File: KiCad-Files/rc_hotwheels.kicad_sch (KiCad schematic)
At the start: 2 parts, among them U1 STM32F070F6P6

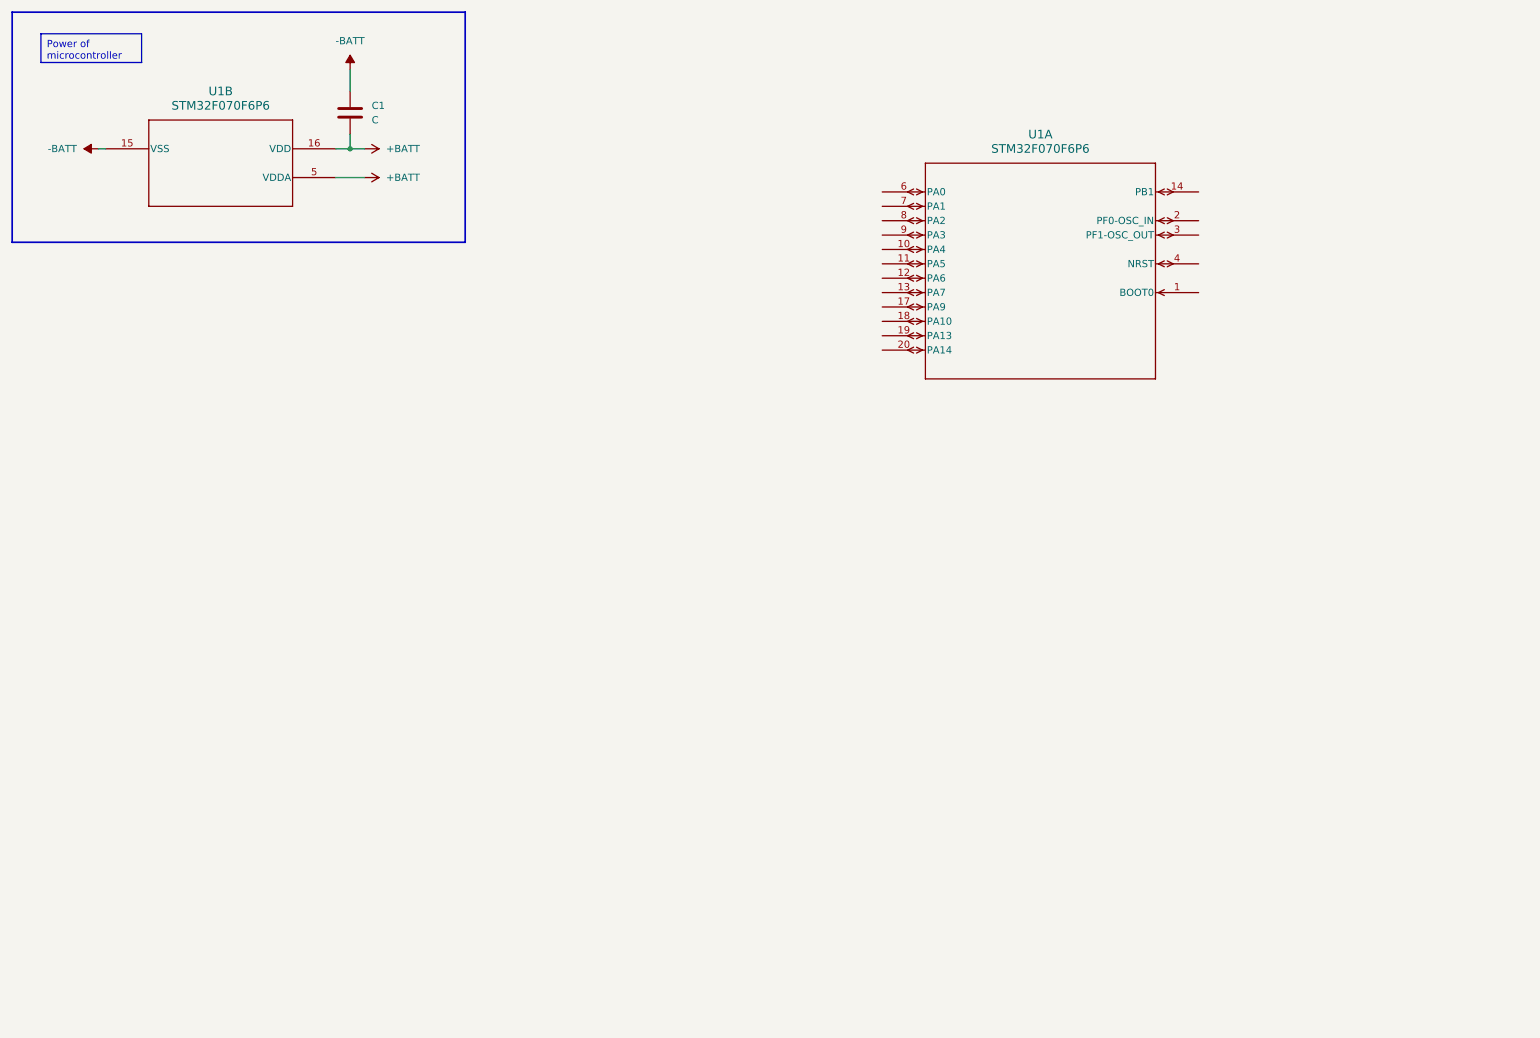
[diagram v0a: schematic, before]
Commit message: Added H-Bridge symbol and connection.
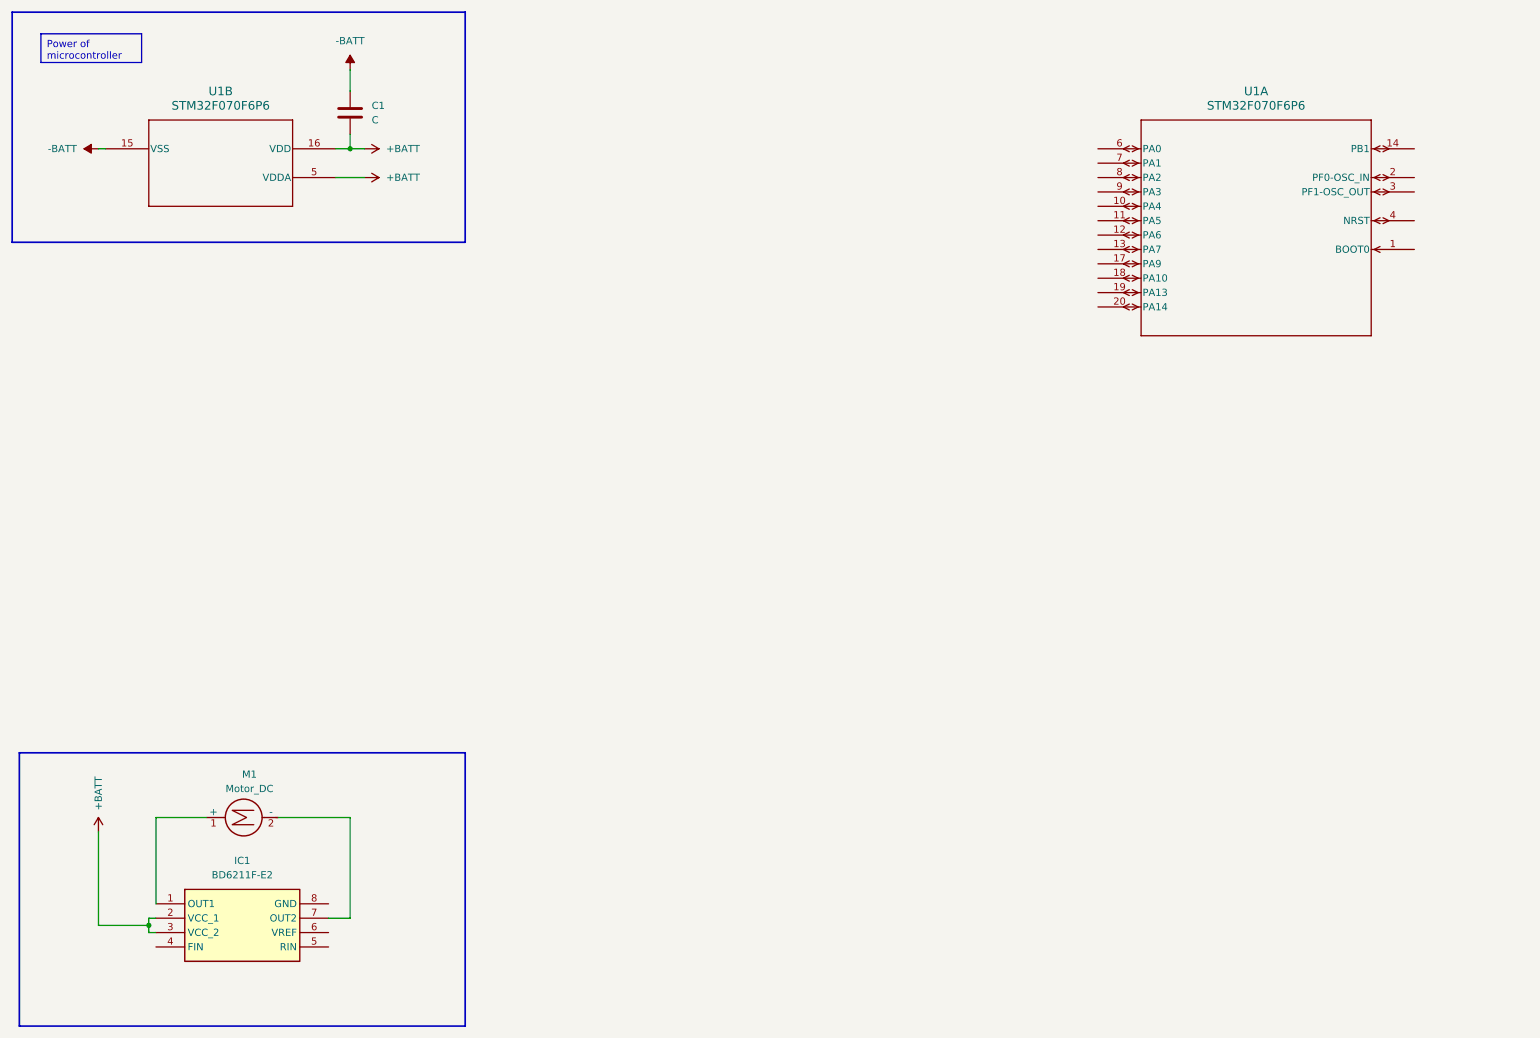
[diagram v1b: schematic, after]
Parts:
- added IC1: BD6211F-E2, SOIC127P620X171-8N, symbol SamacSys_Parts:BD6211F-E2
- added M1: Motor_DC, symbol Motor:Motor_DC
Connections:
- net +BATT: now also IC1.2 (VCC_1), IC1.3 (VCC_2)
- new net: IC1.1 (OUT1), M1.1 (+)
- new net: IC1.7 (OUT2), M1.2 (-)
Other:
- moved on the sheet: U1A
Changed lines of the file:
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@@
   (junction (at 74.93 39.37) (diameter 0) (color 0 0 0 0)
   )
+  (junction (at 39.37 176.53) (diameter 0) (color 0 0 0 0)
+  )
   (wire (pts (xy 74.93 39.37) (xy 77.47 39.37))
     (stroke (width 0) (type default))
   )
+  (wire (pts (xy 71.12 175.26) (xy 74.93 175.26))
+    (stroke (width 0) (type default))
+  )
+  (wire (pts (xy 40.64 172.72) (xy 40.64 157.48))
+    (stroke (width 0) (type default))
+  )
   (wire (pts (xy 74.93 36.83) (xy 74.93 39.37))
     (stroke (width 0) (type default))
@@
     (stroke (width 0) (type default))
   )
+  (wire (pts (xy 39.37 177.8) (xy 39.37 176.53))
+    (stroke (width 0) (type default))
+  )
+  (wire (pts (xy 39.37 175.26) (xy 40.64 175.26))
+    (stroke (width 0) (type default))
+  )
+  (wire (pts (xy 40.64 177.8) (xy 39.37 177.8))
+    (stroke (width 0) (type default))
+  )
+  (wire (pts (xy 39.37 176.53) (xy 39.37 175.26))
+    (stroke (width 0) (type default))
+  )
+  (wire (pts (xy 62.23 157.48) (xy 74.93 157.48))
+    (stroke (width 0) (type default))
+  )
   (wire (pts (xy 72.39 44.45) (xy 77.47 44.45))
     (stroke (width 0) (type default))
   )
+  (wire (pts (xy 40.64 157.48) (xy 49.53 157.48))
+    (stroke (width 0) (type default))
+  )
   (wire (pts (xy 30.48 39.37) (xy 31.75 39.37))
     (stroke (width 0) (type default))
   )
+  (wire (pts (xy 74.93 157.48) (xy 74.93 175.26))
+    (stroke (width 0) (type default))
+  )
+  (wire (pts (xy 30.48 176.53) (xy 39.37 176.53))
+    (stroke (width 0) (type default))
+  )
   (wire (pts (xy 72.39 39.37) (xy 74.93 39.37))
     (stroke (width 0) (type default))
   )
+  (wire (pts (xy 30.48 160.02) (xy 30.48 176.53))
+    (stroke (width 0) (type default))
+  )
   (rectangle (start 15.24 15.24) (end 95.25 55.88)
+    (stroke (width 0.3) (type solid) (color 0 0 0 1))
+    (fill (type none))
+  )
+  (rectangle (start 16.51 146.05) (end 95.25 194.31)
     (stroke (width 0.3) (type solid) (color 0 0 0 1))
     (fill (type none))
@@
     )
   )
-  (symbol (lib_id "2023-11-22_23-54-19:STM32F070F6P6") (at 168.91 46.99 0) (unit 1)
-    (in_bom yes) (on_board yes) (dnp no) (fields_autoplaced)
-    (property "Reference" "U1" (at 196.85 36.83 0)
+  (symbol (lib_id "2023-11-22_23-54-19:STM32F070F6P6") (at 207.01 39.37 0) (unit 1)
+    (in_bom yes) (on_board yes) (dnp no) (fields_autoplaced)
+    (property "Reference" "U1" (at 234.95 29.21 0)
       (effects (font (size 1.524 1.524)))
     )
-    (property "Value" "STM32F070F6P6" (at 196.85 39.37 0)
+    (property "Value" "STM32F070F6P6" (at 234.95 31.75 0)
       (effects (font (size 1.524 1.524)))
     )
-    (property "Footprint" "TSSOP20" (at 168.91 46.99 0)
+    (property "Footprint" "TSSOP20" (at 207.01 39.37 0)
       (effects (font (size 1.27 1.27) italic) hide)
     )
-    (property "Datasheet" "STM32F070F6P6" (at 168.91 46.99 0)
+    (property "Datasheet" "STM32F070F6P6" (at 207.01 39.37 0)
       (effects (font (size 1.27 1.27) italic) hide)
     )
@@
     )
   )
+  (symbol (lib_id "power:+BATT") (at 30.48 160.02 0) (unit 1)
+    (in_bom yes) (on_board yes) (dnp no)
+    (property "Reference" "#PWR05" (at 30.48 163.83 0)
+      (effects (font (size 1.27 1.27)) hide)
+    )
+    (property "Value" "+BATT" (at 30.48 156.21 90)
+      (effects (font (size 1.27 1.27)) (justify left))
+    )
+    (property "Footprint" "" (at 30.48 160.02 0)
+      (effects (font (size 1.27 1.27)) hide)
+    )
+    (property "Datasheet" "" (at 30.48 160.02 0)
+      (effects (font (size 1.27 1.27)) hide)
+    )
+    (pin "1")
+    (instances
+      (project "rc_hotwheels"
+        (path "/0b835094-f9c0-45ab-a312-d1f27d043c8e"
+          (reference "#PWR05") (unit 1)
+        )
+      )
+    )
+  )
+  (symbol (lib_id "Motor:Motor_DC") (at 54.61 157.48 90) (unit 1)
+    (in_bom yes) (on_board yes) (dnp no) (fields_autoplaced)
+    (property "Reference" "M1" (at 57.15 149.86 90)
+      (effects (font (size 1.27 1.27)))
+    )
+    (property "Value" "Motor_DC" (at 57.15 152.4 90)
+      (effects (font (size 1.27 1.27)))
+    )
+    (property "Footprint" "" (at 56.896 157.48 0)
+      (effects (font (size 1.27 1.27)) hide)
+    )
+    (property "Datasheet" "~" (at 56.896 157.48 0)
+      (effects (font (size 1.27 1.27)) hide)
+    )
+    (pin "1")
+    (pin "2")
+    (instances
+      (project "rc_hotwheels"
+        (path "/0b835094-f9c0-45ab-a312-d1f27d043c8e"
+          (reference "M1") (unit 1)
+        )
+      )
+    )
+  )
   (symbol (lib_id "power:-BATT") (at 30.48 39.37 90) (unit 1)
     (in_bom yes) (on_board yes) (dnp no) (fields_autoplaced)
@@
         )
       )
+    )
+  )
+  (symbol (lib_id "SamacSys_Parts:BD6211F-E2") (at 40.64 172.72 0) (unit 1)
+    (in_bom yes) (on_board yes) (dnp no) (fields_autoplaced)
+    (property "Reference" "IC1" (at 55.88 165.1 0)
+      (effects (font (size 1.27 1.27)))
+    )
+    (property "Value" "BD6211F-E2" (at 55.88 167.64 0)
+      (effects (font (size 1.27 1.27)))
+    )
+    (property "Footprint" "SOIC127P620X171-8N" (at 67.31 267.64 0)
+      (effects (font (size 1.27 1.27)) (justify left top) hide)
+    )
+    (property "Datasheet" "https://datasheet.datasheetarchive.com/originals/distributors/Datasheets_SAMA/9ec5cdfbd612023d7489950ca9dee0a8.pdf" (at 67.31 367.64 0)
+      (effects (font (size 1.27 1.27)) (justify left top) hide)
+    )
+    (property "Height" "1.71" (at 67.31 567.64 0)
+      (effects (font (size 1.27 1.27)) (justify left top) hide)
+    )
+    (property "Farnell Part Number" "" (at 67.31 667.64 0)
+      (effects (font (size 1.27 1.27)) (justify left top) hide)
+    )
+    (property "Farnell Price/Stock" "" (at 67.31 767.64 0)
+      (effects (font (size 1.27 1.27)) (justify left top) hide)
+    )
+    (property "Manufacturer_Name" "ROHM Semiconductor" (at 67.31 867.64 0)
+      (effects (font (size 1.27 1.27)) (justify left top) hide)
+    )
+    (property "Manufacturer_Part_Number" "BD6211F-E2" (at 67.31 967.64 0)
+      (effects (font (size 1.27 1.27)) (justify left top) hide)
+    )
+    (pin "1")
+    (pin "2")
+    (pin "3")
+    (pin "4")
+    (pin "5")
+    (pin "6")
+    (pin "7")
+    (pin "8")
+    (instances
+      (project "rc_hotwheels"
+        (path "/0b835094-f9c0-45ab-a312-d1f27d043c8e"
+          (reference "IC1") (unit 1)
+        )
+      )

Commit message: Added receiver symbol and connections
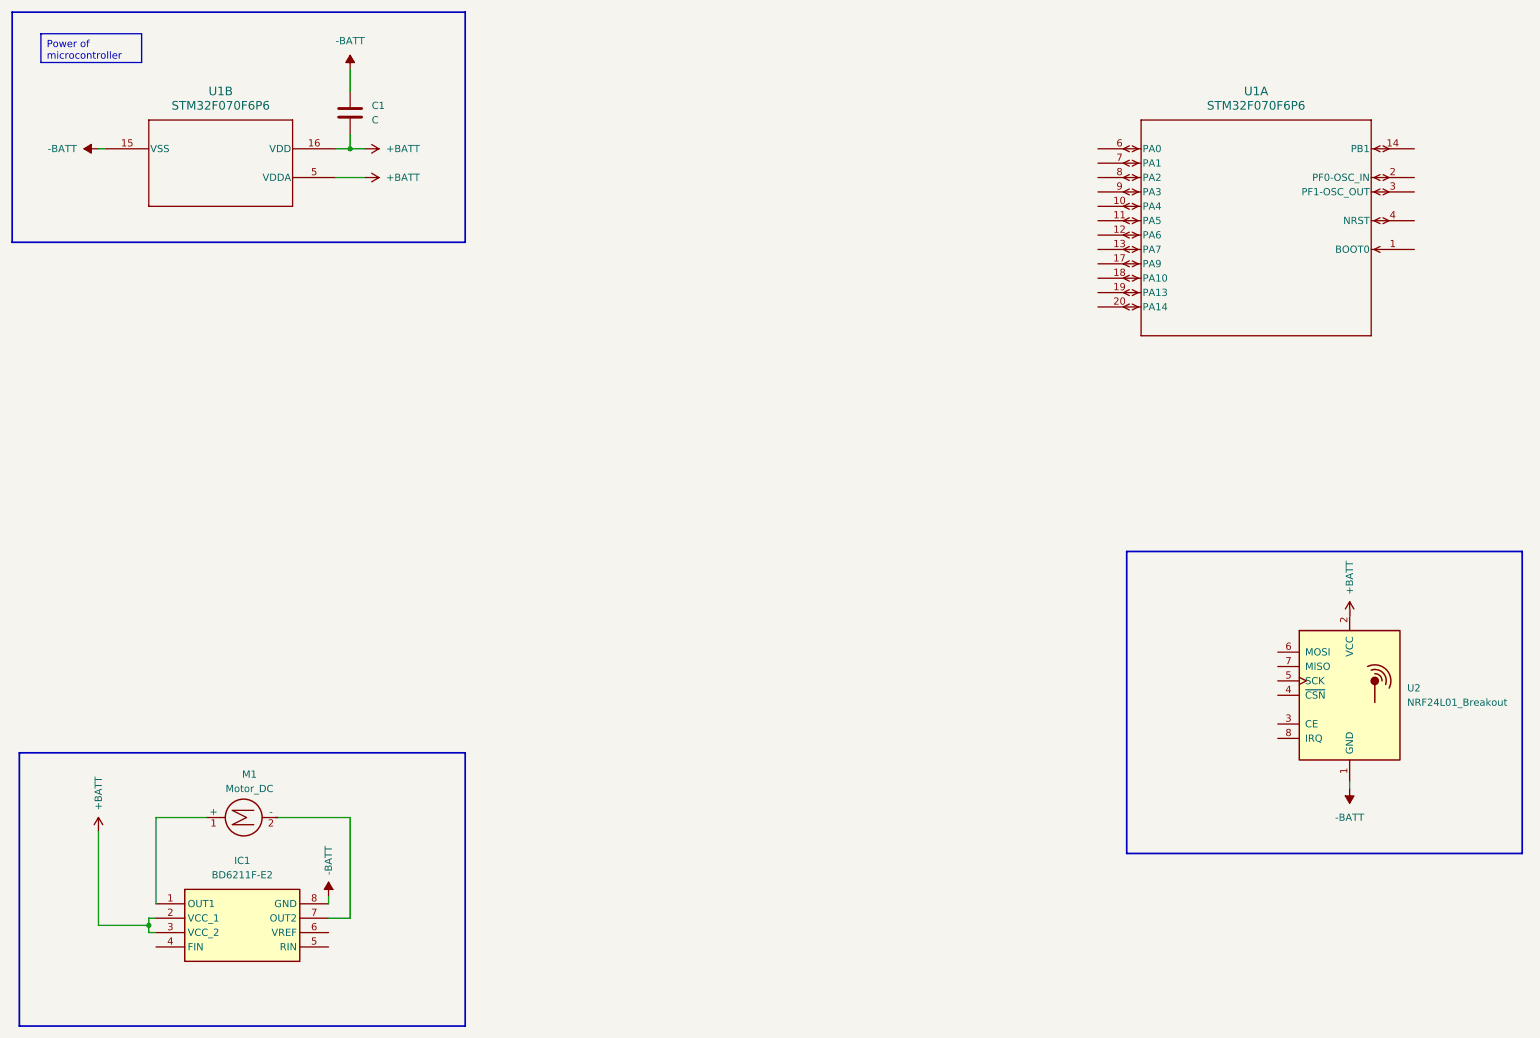
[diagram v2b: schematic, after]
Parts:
- added U2: NRF24L01_Breakout, RF_Module:nRF24L01_Breakout, symbol RF:NRF24L01_Breakout
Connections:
- net +BATT: now also U2.2 (VCC)
- net -BATT: now also IC1.8 (GND), U2.1 (GND)
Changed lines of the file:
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@@
   (junction (at 39.37 176.53) (diameter 0) (color 0 0 0 0)
   )
+  (wire (pts (xy 71.12 171.45) (xy 71.12 172.72))
+    (stroke (width 0) (type default))
+  )
   (wire (pts (xy 74.93 39.37) (xy 77.47 39.37))
     (stroke (width 0) (type default))
@@
     (stroke (width 0) (type default))
   )
+  (wire (pts (xy 251.46 151.13) (xy 251.46 152.4))
+    (stroke (width 0) (type default))
+  )
   (wire (pts (xy 39.37 176.53) (xy 39.37 175.26))
     (stroke (width 0) (type default))
@@
     (stroke (width 0) (type default))
   )
+  (wire (pts (xy 251.46 120.65) (xy 251.46 121.92))
+    (stroke (width 0) (type default))
+  )
   (wire (pts (xy 30.48 39.37) (xy 31.75 39.37))
     (stroke (width 0) (type default))
@@
   (wire (pts (xy 30.48 160.02) (xy 30.48 176.53))
     (stroke (width 0) (type default))
+  )
+  (rectangle (start 212.09 110.49) (end 281.94 163.83)
+    (stroke (width 0.3) (type solid) (color 0 0 0 1))
+    (fill (type none))
   )
   (rectangle (start 15.24 15.24) (end 95.25 55.88)
@@
         (path "/0b835094-f9c0-45ab-a312-d1f27d043c8e"
           (reference "#PWR03") (unit 1)
+        )
+      )
+    )
+  )
+  (symbol (lib_id "power:+BATT") (at 251.46 121.92 0) (unit 1)
+    (in_bom yes) (on_board yes) (dnp no)
+    (property "Reference" "#PWR06" (at 251.46 125.73 0)
+      (effects (font (size 1.27 1.27)) hide)
+    )
+    (property "Value" "+BATT" (at 251.46 118.11 90)
+      (effects (font (size 1.27 1.27)) (justify left))
+    )
+    (property "Footprint" "" (at 251.46 121.92 0)
+      (effects (font (size 1.27 1.27)) hide)
+    )
+    (property "Datasheet" "" (at 251.46 121.92 0)
+      (effects (font (size 1.27 1.27)) hide)
+    )
+    (pin "1")
+    (instances
+      (project "rc_hotwheels"
+        (path "/0b835094-f9c0-45ab-a312-d1f27d043c8e"
+          (reference "#PWR06") (unit 1)
         )
       )
@@
     )
   )
+  (symbol (lib_id "power:-BATT") (at 71.12 171.45 0) (unit 1)
+    (in_bom yes) (on_board yes) (dnp no) (fields_autoplaced)
+    (property "Reference" "#PWR08" (at 71.12 175.26 0)
+      (effects (font (size 1.27 1.27)) hide)
+    )
+    (property "Value" "-BATT" (at 71.12 167.64 90)
+      (effects (font (size 1.27 1.27)) (justify left))
+    )
+    (property "Footprint" "" (at 71.12 171.45 0)
+      (effects (font (size 1.27 1.27)) hide)
+    )
+    (property "Datasheet" "" (at 71.12 171.45 0)
+      (effects (font (size 1.27 1.27)) hide)
+    )
+    (pin "1")
+    (instances
+      (project "rc_hotwheels"
+        (path "/0b835094-f9c0-45ab-a312-d1f27d043c8e"
+          (reference "#PWR08") (unit 1)
+        )
+      )
+    )
+  )
   (symbol (lib_id "Motor:Motor_DC") (at 54.61 157.48 90) (unit 1)
     (in_bom yes) (on_board yes) (dnp no) (fields_autoplaced)
@@
         )
       )
+    )
+  )
+  (symbol (lib_id "RF:NRF24L01_Breakout") (at 251.46 135.89 0) (unit 1)
+    (in_bom yes) (on_board yes) (dnp no) (fields_autoplaced)
+    (property "Reference" "U2" (at 261.62 134.62 0)
+      (effects (font (size 1.27 1.27)) (justify left))
+    )
+    (property "Value" "NRF24L01_Breakout" (at 261.62 137.16 0)
+      (effects (font (size 1.27 1.27)) (justify left))
+    )
+    (property "Footprint" "RF_Module:nRF24L01_Breakout" (at 255.27 120.65 0)
+      (effects (font (size 1.27 1.27) italic) (justify left) hide)
+    )
+    (property "Datasheet" "http://www.nordicsemi.com/eng/content/download/2730/34105/file/nRF24L01_Product_Specification_v2_0.pdf" (at 251.46 138.43 0)
+      (effects (font (size 1.27 1.27)) hide)
+    )
+    (pin "1")
+    (pin "2")
+    (pin "3")
+    (pin "4")
+    (pin "5")
+    (pin "6")
+    (pin "7")
+    (pin "8")
+    (instances
+      (project "rc_hotwheels"
+        (path "/0b835094-f9c0-45ab-a312-d1f27d043c8e"
+          (reference "U2") (unit 1)
+        )
+      )
+    )
+  )
+  (symbol (lib_id "power:-BATT") (at 251.46 152.4 180) (unit 1)
+    (in_bom yes) (on_board yes) (dnp no) (fields_autoplaced)
+    (property "Reference" "#PWR07" (at 251.46 148.59 0)
+      (effects (font (size 1.27 1.27)) hide)
+    )
+    (property "Value" "-BATT" (at 251.46 157.48 0)
+      (effects (font (size 1.27 1.27)))
+    )
+    (property "Footprint" "" (at 251.46 152.4 0)
+      (effects (font (size 1.27 1.27)) hide)
+    )
+    (property "Datasheet" "" (at 251.46 152.4 0)
+      (effects (font (size 1.27 1.27)) hide)
+    )
+    (pin "1")
+    (instances
+      (project "rc_hotwheels"
+        (path "/0b835094-f9c0-45ab-a312-d1f27d043c8e"
+          (reference "#PWR07") (unit 1)
+        )
+      )
